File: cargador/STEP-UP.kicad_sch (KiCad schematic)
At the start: 7 parts, among them U1 MT3608

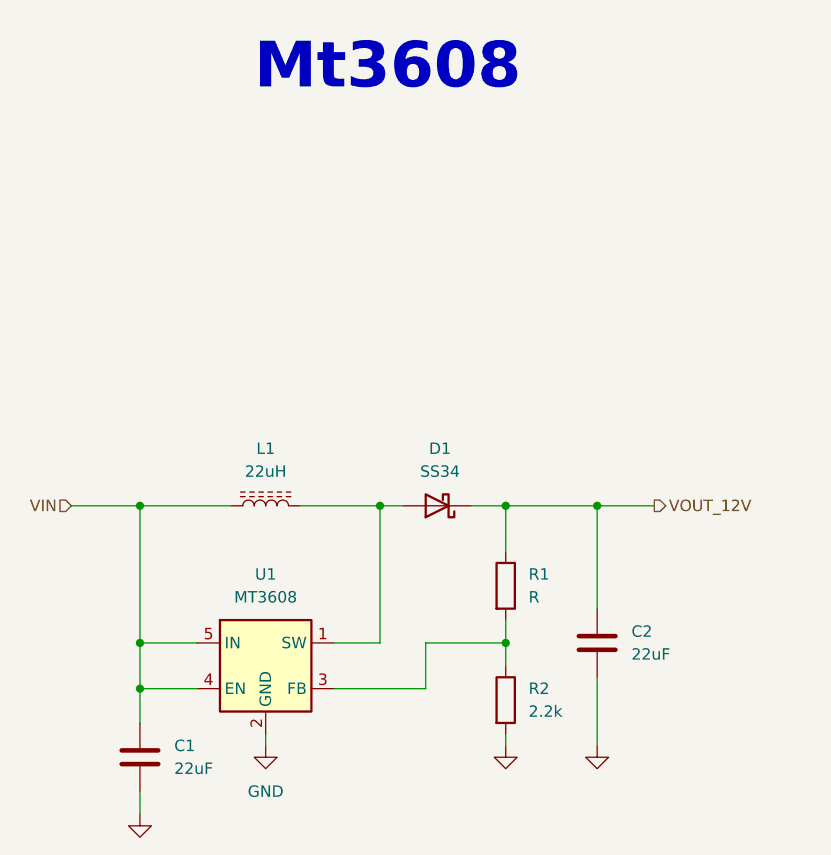
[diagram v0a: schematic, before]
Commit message: parcialmente terminada PCB falta verificar tamano de componentes
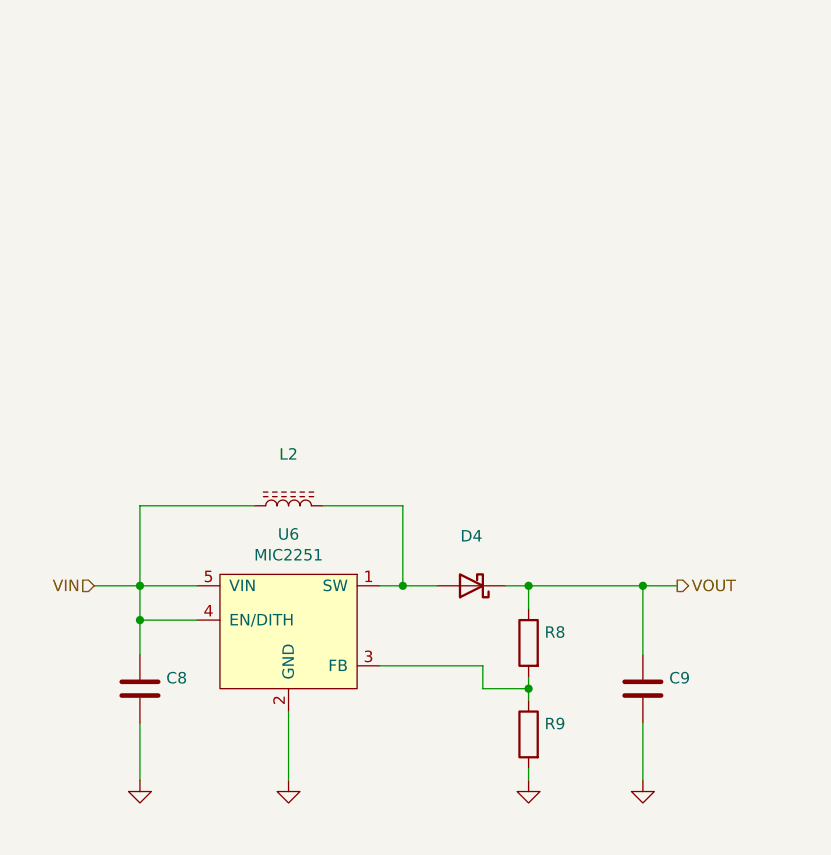
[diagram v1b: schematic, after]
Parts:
- removed C1: 22uF, Capacitor_SMD:C_0603_1608Metric, symbol Device:C
- removed C2: 22uF, Capacitor_SMD:C_0805_2012Metric_Pad1.18x1.45mm_HandSolder, symbol Device:C
- removed D1: SS34, Diode_SMD:D_SOD-123, symbol Device:D_Schottky
- removed L1: 22uH, MSS_Devices:L_Bourns_SDR0403, symbol Device:L_Ferrite
- removed R1: R, Resistor_SMD:R_0603_1608Metric, symbol Device:R
- removed R2: 2.2k, Resistor_SMD:R_0603_1608Metric, symbol Device:R
- removed U1: MT3608, Package_TO_SOT_SMD:SOT-23-6, symbol Regulator_Switching:MT3608
- added C8: ~, Capacitor_SMD:C_0603_1608Metric, symbol Device:C
- added C9: (no value), symbol Device:C
- added D4: ~, Diode_SMD:D_SOD-123, symbol Device:D_Schottky
- added L2: ~, MSS_Devices:L_Bourns_SDR0403, symbol Device:L_Ferrite
- added R8, R9: ~, Resistor_SMD:R_0603_1608Metric, symbol Device:R
- added U6: MIC2251, Package_TO_SOT_SMD:SOT-23-5, symbol cargadorDeBateriasLitIon-rescue:MIC2251-MSS_SourceSwitch
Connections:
- net GND: now also C8.2, C9.2, R9.2, U6.2 (GND)
- net VIN: now also C8.1, L2.1, U6.4 (EN/DITH), U6.5 (VIN)
- new net: D4.2 (A), L2.2, U6.1 (SW)
- new net: R8.2, R9.1, U6.3 (FB)
- new net VOUT: C9.1, D4.1 (K), R8.1
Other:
- note removed: "Mt3608"

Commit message: terminando, aun falta una ultima revision previa a la fabricacion
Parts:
- removed U6: MIC2251, Package_TO_SOT_SMD:SOT-23-5, symbol cargadorDeBateriasLitIon-rescue:MIC2251-MSS_SourceSwitch
- added R12: 2.2k, Resistor_SMD:R_0603_1608Metric, symbol Device:R
- added U6: SDB628, Package_TO_SOT_SMD:SOT-23-6, symbol Regulator_Switching:MT3608
- C8: value ~ -> 22uF; footprint Capacitor_SMD:C_0603_1608Metric -> Capacitor_SMD:C_1206_3216Metric; Mfg Part # GRM21BR61E106KA73L -> (none)
- C9: value (none) -> 22uF; footprint (none) -> Capacitor_SMD:C_1206_3216Metric
- D4: value ~ -> SS34; footprint Diode_SMD:D_SOD-123 -> Diode_SMD:D_SMB; Mfg Part # SM5819PL-TP -> (none)
- L2: value ~ -> 22uH; footprint MSS_Devices:L_Bourns_SDR0403 -> MSS_Devices:L_Bourns-SDE0805A_7x7.8mm; Mfg Part # SDR0403-100ML -> (none)
- R8: value ~ -> 10K; Mfg Part # RC0603FR-07100KL -> (none)
- R9: value ~ -> 6.2K; Mfg Part # RC0603FR-0733KL -> (none)
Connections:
- net GND: now also R12.2, U6.2 (GND); no longer R9.2
- net VIN: now also U6.4 (EN), U6.5 (IN)
- net at D4.2 (A), L2.2: now also U6.1 (SW)
- new net: R12.1, R9.2, U6.3 (FB)
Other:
- note added: "Vo=0.6x[1+((R1+R11)/R2)]"
